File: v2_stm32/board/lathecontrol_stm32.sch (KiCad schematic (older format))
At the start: 18 parts

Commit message: STM32 board: Power supply
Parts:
- removed C? (x2): 100n, Capacitor_SMD:C_0603_1608Metric, symbol Device:C
- removed C?: 2u2, Capacitor_SMD:C_0603_1608Metric, symbol Device:C
- removed C?: 22u, Capacitor_SMD:C_0805_2012Metric, symbol Device:C
- removed D?: D, Diode_SMD:D_SOD-123F, symbol Device:D
- removed R?: 240, Resistor_SMD:R_0603_1608Metric, symbol Device:R
- removed R?: 82, Resistor_SMD:R_0603_1608Metric, symbol Device:R
- removed U?: LM317_TO-252, Package_TO_SOT_SMD:TO-252-2, symbol Regulator_Linear:LM317_TO-252
- removed U?: AMS1117-3.3, Package_TO_SOT_SMD:SOT-223-3_TabPin2, symbol Regulator_Linear:AMS1117-3.3
- added R?: 1k5, Resistor_SMD:R_0603_1608Metric, symbol Device:R
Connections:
- net labels added: BOOT0, NRST, SWCLK, SWDIO, TRACE_SWO, USB_D+, USB_D-
- net labels removed: +1V8, VADJ_1V8, VCC
- wire segments 75 -> 49
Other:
- note removed: "Measuring stick voltage supply (1.7 V)"
- note removed: "Todo: Low pass filter?"

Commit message: Switched to 64 pin STM32F103. Assigned pins
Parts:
- removed U?: STM32F103CBTx, Package_QFP:LQFP-48_7x7mm_P0.5mm, symbol MCU_ST_STM32F1:STM32F103CBTx
- added C?: 100n, Capacitor_SMD:C_0603_1608Metric, symbol Device:C
- added U?: STM32F103RBTx, Package_QFP:LQFP-64_10x10mm_P0.5mm, symbol MCU_ST_STM32F1:STM32F103RBTx
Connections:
- net labels added: ADC1, ADC2, ADC3, ADC4, BTN1, BTN2, BTN3, BTN4, DISPL_CS, DISPL_DC, DISPL_MISO, DISPL_MOSI, DISPL_RST, DISPL_SCK, DISPL_T_CS, DISPL_T_IRQ, ENC_1, ENC_2, ENC_BTN, GPIO1, GPIO2, I2C_SCL, I2C_SDA, MS1_CLK, MS1_DAT, MS2_CLK, MS2_DAT, MS3_CLK, MS3_DAT, MS4_CLK, MS4_DAT, ROT1, SPI_MISO, SPI_MOSI, SPI_SCK, SPI_SS0, SPI_SS1, UART_RX, UART_TX
- wire segments 49 -> 61
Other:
- moved on the sheet: C?, R?, Y?

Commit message: Pins
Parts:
- added C9: 100n, Capacitor_SMD:C_0603_1608Metric, symbol Device:C
- added J1, J3: Conn_01x04_Male, symbol Connector:Conn_01x04_Male
- added J2: Conn_01x07_Male, symbol Connector:Conn_01x07_Male
- added J4: USB_B_Micro, symbol Connector:USB_B_Micro
- added J5, J6: Conn_01x05_Male, symbol Connector:Conn_01x05_Male
- added J7: Conn_01x14_Female, symbol Connector:Conn_01x14_Female
- added J8: Conn_01x06_Male, symbol Connector:Conn_01x06_Male
- gave numbers to parts that had none: 11
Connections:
- net labels added: +5V
- wire segments 61 -> 73
- no-connect marks 0 -> 8
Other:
- note added: "Programming Interface"
- note added: "Touchdisplay Connector"
- note added: "https://www.aliexpress.com/item/4001122632293.html"
- moved on the sheet: C1, C2, C3, C4, C5, C6, C7, C8, R1, U1, Y1

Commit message: Added connectors
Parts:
- removed J1, J3: Conn_01x04_Male, symbol Connector:Conn_01x04_Male
- removed J2: Conn_01x07_Male, symbol Connector:Conn_01x07_Male
- removed J8: Conn_01x06_Male, symbol Connector:Conn_01x06_Male
- added J1, J2: Conn_01x05_Male, symbol Connector:Conn_01x05_Male
- added J3: Barrel_Jack_Switch, symbol Connector:Barrel_Jack_Switch
- added J8: Conn_01x24, Lathecontrol_STM32:FFC_FPC_1x24_DualSide_JUSHUO_AFC24-S24FIC-00, symbol Connector_Generic:Conn_01x24
- added R1: 10k, Resistor_SMD:R_0603_1608Metric, symbol Device:R
- J4: symbol Connector:USB_B_Micro -> lathecontrol_stm32-rescue:USB_B_Micro-Connector
- renumbered C7 to C1, C8 to C2, C1 to C3, C2 to C4, C3 to C5, C4 to C6, C5 to C7, C6 to C8, J6 to J5, J5 to J6, R1 to R2
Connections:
- net labels added: VCC
- wire segments 73 -> 105
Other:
- moved on the sheet: J5, J6

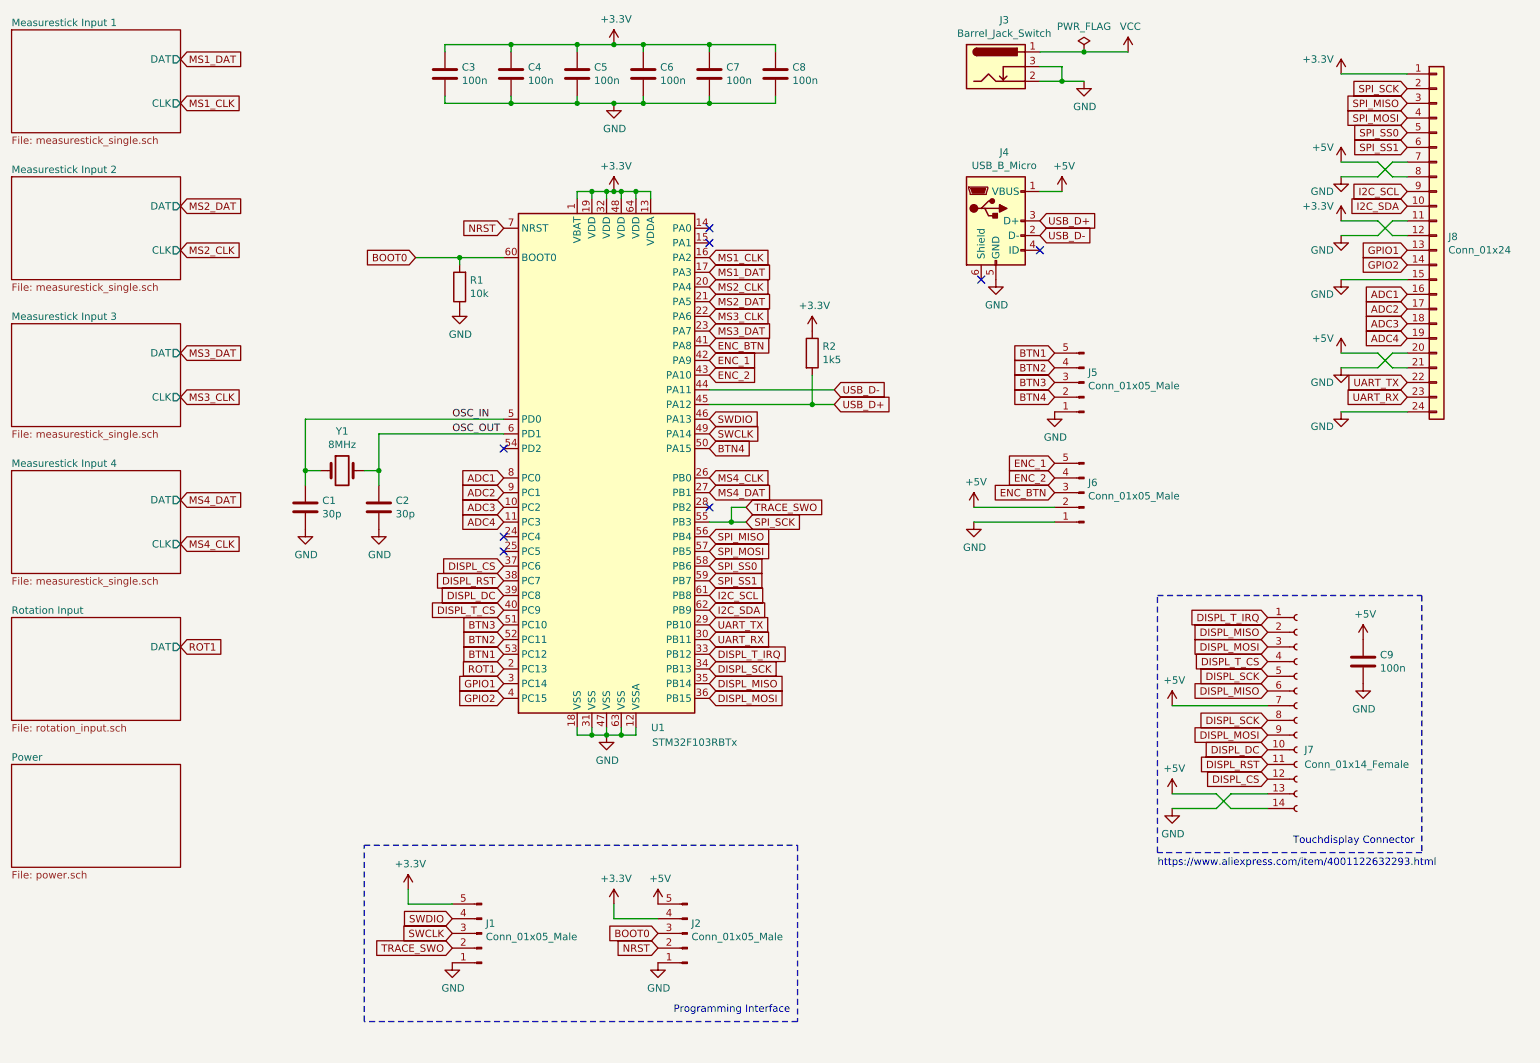
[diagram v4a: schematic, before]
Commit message: Added LEDs
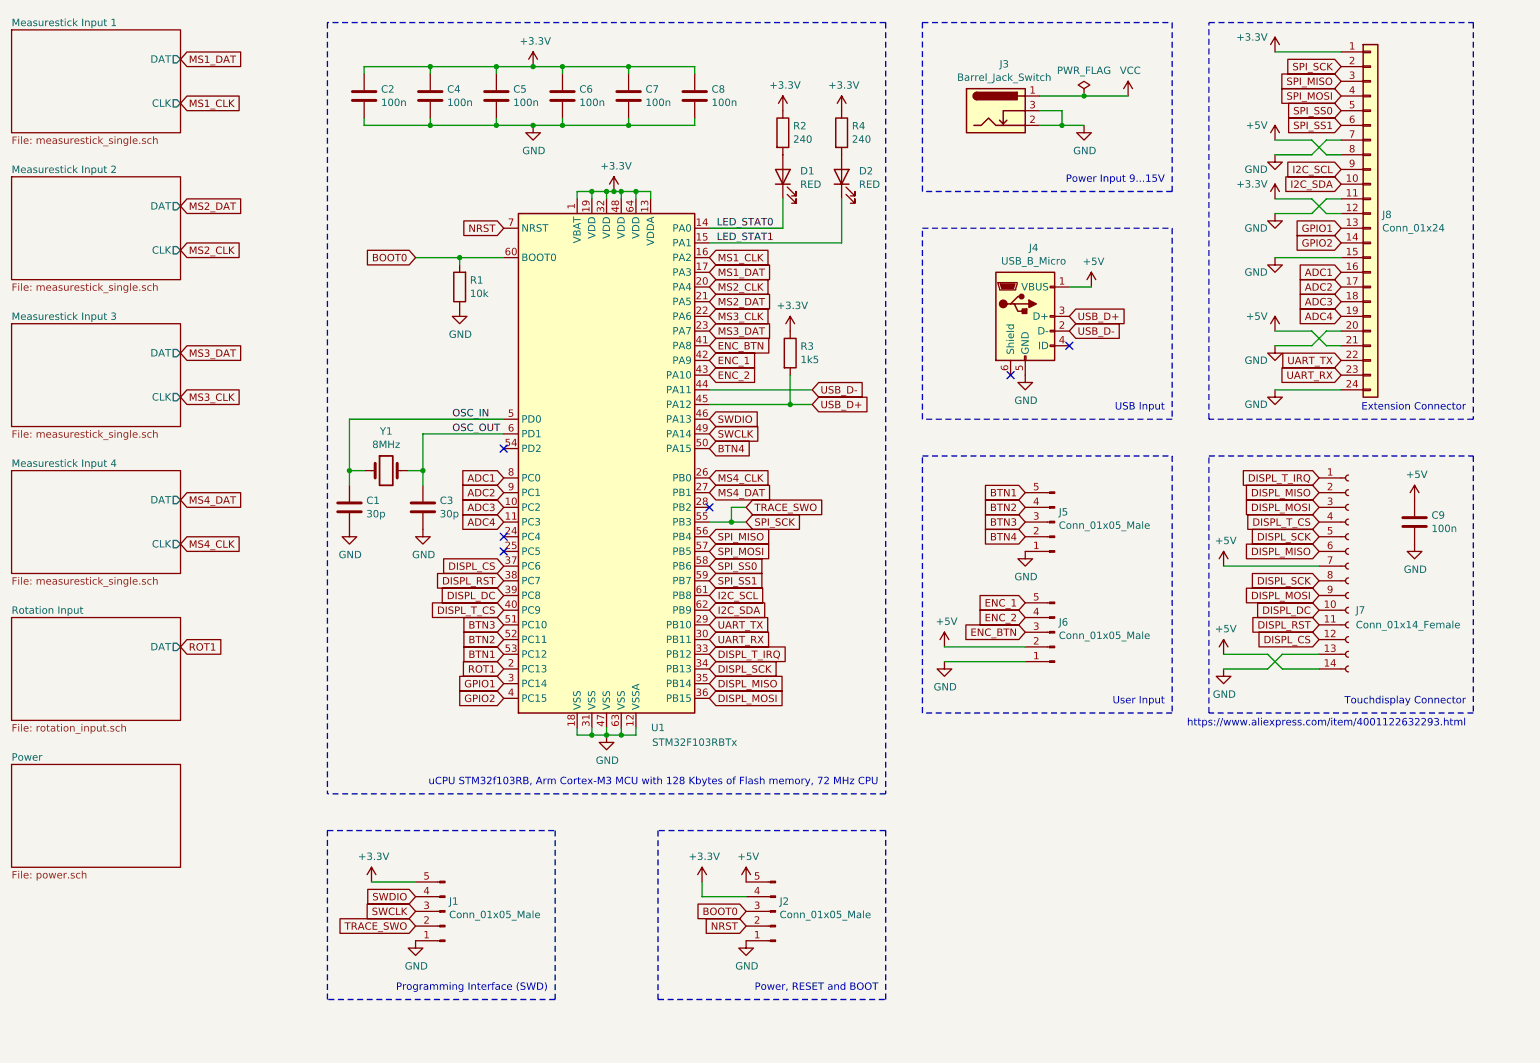
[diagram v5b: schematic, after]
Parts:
- added D1, D2: RED, LED_SMD:LED_0603_1608Metric, symbol Device:LED
- added R2, R4: 240, Resistor_SMD:R_0603_1608Metric, symbol Device:R
- renumbered C3 to C2, C2 to C3, R2 to R3
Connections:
- net +3V3: now also R2.1, R4.1
- net LED_STAT0: now reaches U1.14 (PA0)
- net LED_STAT0: now also D1.1 (K)
- net LED_STAT1: now reaches U1.15 (PA1)
- net LED_STAT1: now also D2.1 (K)
- new net: D1.2 (A), R2.2
- new net: D2.2 (A), R4.2
- no-connect marks 8 -> 6
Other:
- note added: "Extension Connector"
- note added: "Power Input 9...15V"
- note added: "Power, RESET and BOOT"
- note added: "Programming Interface (SWD)"
- note added: "USB Input"
- note added: "User Input"
- note added: "uCPU STM32f103RB, Arm Cortex-M3 MCU with 128 Kbytes of Flash memory, 72 MHz CPU"
- note removed: "Programming Interface"
- moved on the sheet: C1, C2, C3, C4, C5, C6, C7, C8, C9, J1, J2, J3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

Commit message: Schematic finished (V0.1), Added footprints
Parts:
- J1, J2, J5, J6: footprint (none) -> Connector_PinHeader_2.54mm:PinHeader_1x05_P2.54mm_Vertical
- J3: footprint (none) -> Lathecontrol_STM32:BarrelJack_Horizontal_DC-005-20A; LCSC (none) -> C136744
- J4: footprint (none) -> Lathecontrol_STM32:USB_Micro-B_SHOU_HAN_MicroXNJ; LCSC (none) -> C404969
- J7: footprint (none) -> Connector_PinHeader_2.54mm:PinHeader_1x14_P2.54mm_Vertical
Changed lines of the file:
@@
 F 0 "J7" H 9900 4100 50  0000 L CNN
 F 1 "Conn_01x14_Female" H 9900 4000 50  0000 L CNN
-F 2 "" H 9850 4400 50  0001 C CNN
+F 2 "Connector_PinHeader_2.54mm:PinHeader_1x14_P2.54mm_Vertical" H 9850 4400 50  0001 C CNN
 F 3 "~" H 9850 4400 50  0001 C CNN
 	1    9850 4400
@@
 F 0 "J6" H 7822 4782 50  0000 R CNN
 F 1 "Conn_01x05_Male" H 7822 4873 50  0000 R CNN
-F 2 "" H 7850 4850 50  0001 C CNN
+F 2 "Connector_PinHeader_2.54mm:PinHeader_1x05_P2.54mm_Vertical" H 7850 4850 50  0001 C CNN
 F 3 "~" H 7850 4850 50  0001 C CNN
 	1    7850 4850
@@
 F 0 "J5" H 7822 4032 50  0000 R CNN
 F 1 "Conn_01x05_Male" H 7822 4123 50  0000 R CNN
-F 2 "" H 7850 4100 50  0001 C CNN
+F 2 "Connector_PinHeader_2.54mm:PinHeader_1x05_P2.54mm_Vertical" H 7850 4100 50  0001 C CNN
 F 3 "~" H 7850 4100 50  0001 C CNN
 	1    7850 4100
@@
 F 0 "J4" H 7707 3167 50  0000 C CNN
 F 1 "USB_B_Micro" H 7707 3076 50  0000 C CNN
-F 2 "" H 7800 2650 50  0001 C CNN
-F 3 "~" H 7800 2650 50  0001 C CNN
+F 2 "Lathecontrol_STM32:USB_Micro-B_SHOU_HAN_MicroXNJ" H 7800 2650 50  0001 C CNN
+F 3 "https://datasheet.lcsc.com/szlcsc/1912111437_SHOU-HAN-MicroXNJ_C404969.pdf" H 7800 2650 50  0001 C CNN
+F 4 "C404969" H 7650 2700 50  0001 C CNN "LCSC"
 	1    7650 2700
 	1    0    0    -1
@@
 F 1 "Conn_01x24" H 10080 1901 50  0000 L CNN
 F 2 "Lathecontrol_STM32:FFC_FPC_1x24_DualSide_JUSHUO_AFC24-S24FIC-00" H 10000 2000 50  0001 C CNN
-F 3 "1811021330_JUSHUO-AFC24-S24FIC-00_C262292.pdf" H 10000 2000 50  0001 C CNN
+F 3 "https://datasheet.lcsc.com/szlcsc/1811021330_JUSHUO-AFC24-S24FIC-00_C262292.pdf" H 10000 2000 50  0001 C CNN
 F 4 "C262292" H 10000 2000 50  0001 C CNN "LCSC"
 	1    10000 2000
@@
 F 0 "J3" H 7507 1617 50  0000 C CNN
 F 1 "Barrel_Jack_Switch" H 7507 1526 50  0000 C CNN
-F 2 "" H 7500 1260 50  0001 C CNN
-F 3 "~" H 7500 1260 50  0001 C CNN
+F 2 "Lathecontrol_STM32:BarrelJack_Horizontal_DC-005-20A" H 7500 1260 50  0001 C CNN
+F 3 "https://datasheet.lcsc.com/szlcsc/1811082118_Korean-Hroparts-Elec-DC-005-20A_C136744.pdf" H 7500 1260 50  0001 C CNN
+F 4 "C136744" H 7450 1300 50  0001 C CNN "LCSC"
 	1    7450 1300
 	1    0    0    -1
@@
 F 0 "J2" H 5922 6682 50  0000 R CNN
 F 1 "Conn_01x05_Male" H 5922 6773 50  0000 R CNN
-F 2 "" H 5950 6750 50  0001 C CNN
+F 2 "Connector_PinHeader_2.54mm:PinHeader_1x05_P2.54mm_Vertical" H 5950 6750 50  0001 C CNN
 F 3 "~" H 5950 6750 50  0001 C CNN
 	1    5950 6750
@@
 F 0 "J1" H 3672 6682 50  0000 R CNN
 F 1 "Conn_01x05_Male" H 3672 6773 50  0000 R CNN
-F 2 "" H 3700 6750 50  0001 C CNN
+F 2 "Connector_PinHeader_2.54mm:PinHeader_1x05_P2.54mm_Vertical" H 3700 6750 50  0001 C CNN
 F 3 "~" H 3700 6750 50  0001 C CNN
 	1    3700 6750

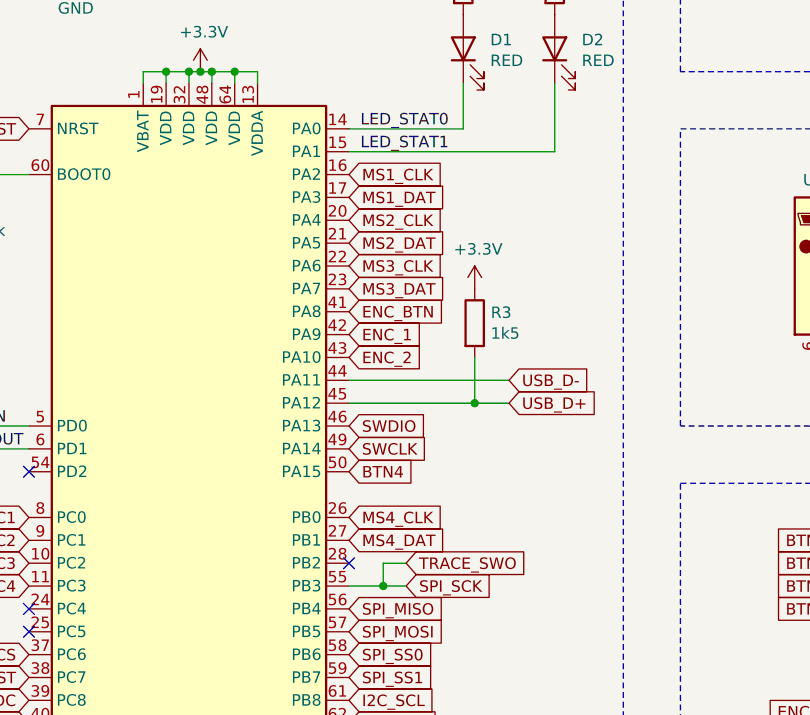
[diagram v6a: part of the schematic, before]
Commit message: Changed MS DAT/CLK pins. Routed measuring stick input
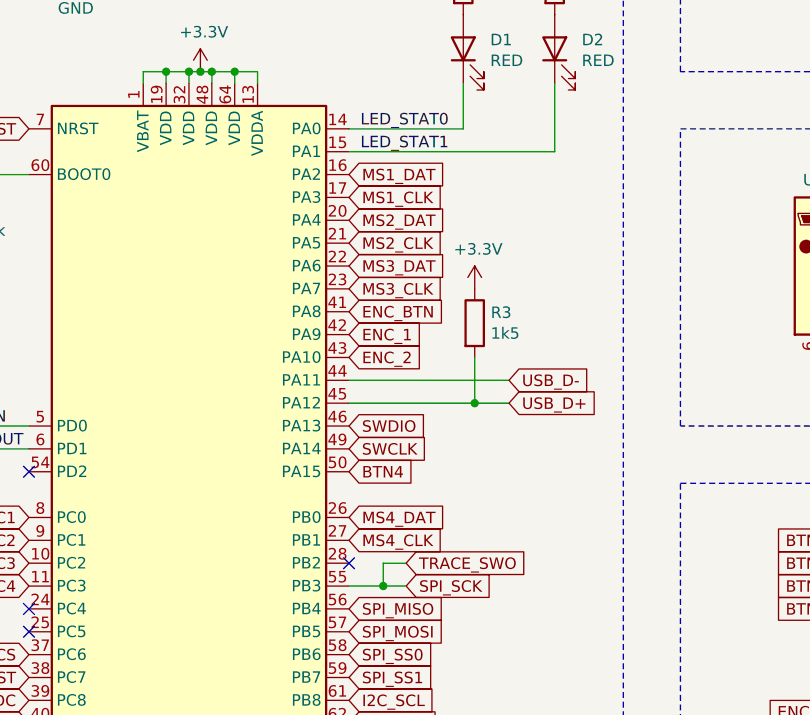
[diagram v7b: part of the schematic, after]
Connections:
- net MS1_CLK: now also U1.17 (PA3); no longer U1.16 (PA2)
- net MS1_DAT: now also U1.16 (PA2); no longer U1.17 (PA3)
- net MS2_CLK: now also U1.21 (PA5); no longer U1.20 (PA4)
- net MS2_DAT: now also U1.20 (PA4); no longer U1.21 (PA5)
- net MS3_CLK: now also U1.23 (PA7); no longer U1.22 (PA6)
- net MS3_DAT: now also U1.22 (PA6); no longer U1.23 (PA7)
- net MS4_CLK: now also U1.27 (PB1); no longer U1.26 (PB0)
- net MS4_DAT: now also U1.26 (PB0); no longer U1.27 (PB1)
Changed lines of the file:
@@
 Text GLabel 5500 5200 2    50   Input ~ 0
 DISPL_MISO
+Text GLabel 5500 3900 2    50   Input ~ 0
+MS4_CLK
 Text GLabel 5500 3800 2    50   Input ~ 0
-MS4_CLK
-Text GLabel 5500 3900 2    50   Input ~ 0
 MS4_DAT
 Text GLabel 1900 4250 2    50   Input ~ 0
@@
 Text GLabel 1900 3950 2    50   Input ~ 0
 MS4_DAT
+Text GLabel 5500 2400 2    50   Input ~ 0
+MS1_CLK
 Text GLabel 5500 2300 2    50   Input ~ 0
-MS1_CLK
-Text GLabel 5500 2400 2    50   Input ~ 0
 MS1_DAT
+Text GLabel 5500 2600 2    50   Input ~ 0
+MS2_CLK
 Text GLabel 5500 2500 2    50   Input ~ 0
-MS2_CLK
-Text GLabel 5500 2600 2    50   Input ~ 0
 MS2_DAT
+Text GLabel 5500 2800 2    50   Input ~ 0
+MS3_CLK
 Text GLabel 5500 2700 2    50   Input ~ 0
-MS3_CLK
-Text GLabel 5500 2800 2    50   Input ~ 0
 MS3_DAT
 Text GLabel 1900 1250 2    50   Input ~ 0

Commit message: More PCB design
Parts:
- removed C8, C9: 100n, Capacitor_SMD:C_0603_1608Metric, symbol Device:C
- removed D1: RED, LED_SMD:LED_0603_1608Metric, symbol Device:LED
- removed J1, J2: Conn_01x05_Male, Connector_PinHeader_2.54mm:PinHeader_1x05_P2.54mm_Vertical, symbol Connector:Conn_01x05_Male
- removed R2: 240, Resistor_SMD:R_0603_1608Metric, symbol Device:R
- added H1, H2, H3, H4, H5, H6: MountingHole_Pad, MountingHole:MountingHole_3mm_Pad, symbol Mechanical:MountingHole_Pad
- added J1: Conn_01x06_Male, Connector_PinHeader_2.54mm:PinHeader_1x06_P2.54mm_Vertical, symbol Connector:Conn_01x06_Male
- added JP1: BOOTSEL, Connector_PinHeader_2.54mm:PinHeader_1x02_P2.54mm_Horizontal, symbol Jumper:Jumper_2_Open
- J5: footprint Connector_PinHeader_2.54mm:PinHeader_1x05_P2.54mm_Vertical -> Connector_PinHeader_2.54mm:PinHeader_1x06_P2.54mm_Horizontal
- J6: footprint Connector_PinHeader_2.54mm:PinHeader_1x05_P2.54mm_Vertical -> Connector_PinHeader_2.54mm:PinHeader_1x05_P2.54mm_Horizontal
- J7: footprint Connector_PinHeader_2.54mm:PinHeader_1x14_P2.54mm_Vertical -> Connector_PinSocket_2.54mm:PinSocket_1x14_P2.54mm_Vertical
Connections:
- net +3V3: now also J6.2 (Pin_2), JP1.1 (A); no longer R4.1, U1.13 (VDDA)
- net +5V: no longer J4.1 (VBUS), J6.2 (Pin_2), J7.7 (Pin_7)
- net BOOT0: now also JP1.2 (B)
- net BTN1: now also J5.2 (Pin_2), U1.57 (PB5); no longer J5.5 (Pin_5), U1.53 (PC12)
- net BTN2: now also J5.3 (Pin_3), U1.56 (PB4); no longer J5.4 (Pin_4), U1.52 (PC11)
- net BTN3: now also J5.4 (Pin_4), U1.52 (PC11); no longer J5.3 (Pin_3), U1.51 (PC10)
- net BTN4: now also J5.5 (Pin_5), U1.51 (PC10); no longer J5.2 (Pin_2), U1.50 (PA15)
- net DISPL_T_IRQ: now also U1.30 (PB11); no longer U1.33 (PB12)
- net GND: now also D2.1 (K), H1.1, H2.1, H3.1, H4.1, H5.1, H6.1, J1.3 (Pin_3)
- net LED_STAT1: now also R4.1; no longer D2.1 (K)
- net NRST: now also J1.5 (Pin_5)
- net SWCLK: now also J1.2 (Pin_2)
- net SWDIO: now also J1.4 (Pin_4)
- net UART_RX: now also U1.59 (PB7); no longer U1.30 (PB11)
- net UART_TX: now also U1.58 (PB6); no longer U1.29 (PB10)
- net GPIO1: no longer names the net of U1.3 (PC14)
- net GPIO1: no longer J8.13 (Pin_13)
- net GPIO2: no longer names the net of U1.4 (PC15)
- net GPIO2: no longer J8.14 (Pin_14)
- net LED_STAT0: no longer names the net of U1.14 (PA0)
- net SPI_MISO: no longer names the net of J8.3 (Pin_3)
- net SPI_MISO: no longer U1.56 (PB4)
- net SPI_MOSI: no longer names the net of J8.4 (Pin_4)
- net SPI_MOSI: no longer U1.57 (PB5)
- net SPI_SCK: no longer names the net of J8.2 (Pin_2)
- net SPI_SCK: no longer U1.55 (PB3)
- net SPI_SS0: no longer names the net of J8.5 (Pin_5)
- net SPI_SS0: no longer U1.58 (PB6)
- net SPI_SS1: no longer names the net of J8.6 (Pin_6)
- net SPI_SS1: no longer U1.59 (PB7)
- net VCC renamed IN_VCC
- new net +3.3VA: U1.13 (VDDA)
- new net DISPL_LED: J7.7 (Pin_7), U1.29 (PB10)
- new net IN_+5V: J1.1 (Pin_1), J4.1 (VBUS)
- new net SWD_SWO: J1.6 (Pin_6), U1.55 (PB3)
- no-connect marks 6 -> 19
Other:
- note added: "C1 = C3 = 2 * (CL - Cstray)\nCL = 20 pF (Cystal Datasheet)\nCstray ca. 5 pF"
- note added: "PC13, PC14, PC15 \ncan source / sink \n+/-3mA only!\n"
- note removed: "Power, RESET and BOOT"
- moved on the sheet: D2, R1, R4
